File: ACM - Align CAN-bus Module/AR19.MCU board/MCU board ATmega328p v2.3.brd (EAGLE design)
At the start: 33.3 x 30.8 mm, 37 parts, among them IC1 ATMEGA328P-MMH, IC2 MIC5239-5.0YS_TR, IC3 MCP25625-E_ML, J1 AVR_SPI_PROG_3X2NS

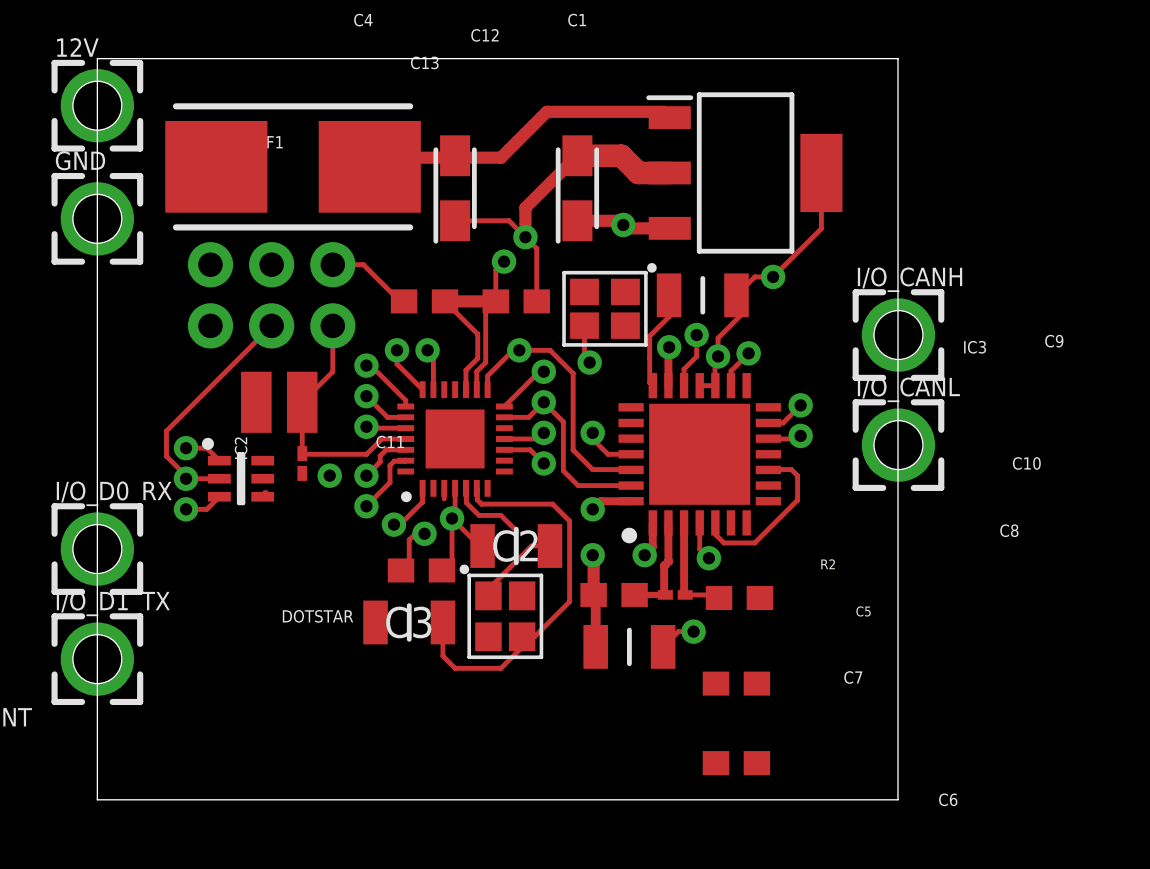
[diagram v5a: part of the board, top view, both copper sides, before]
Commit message: Removed: Extra GND connections
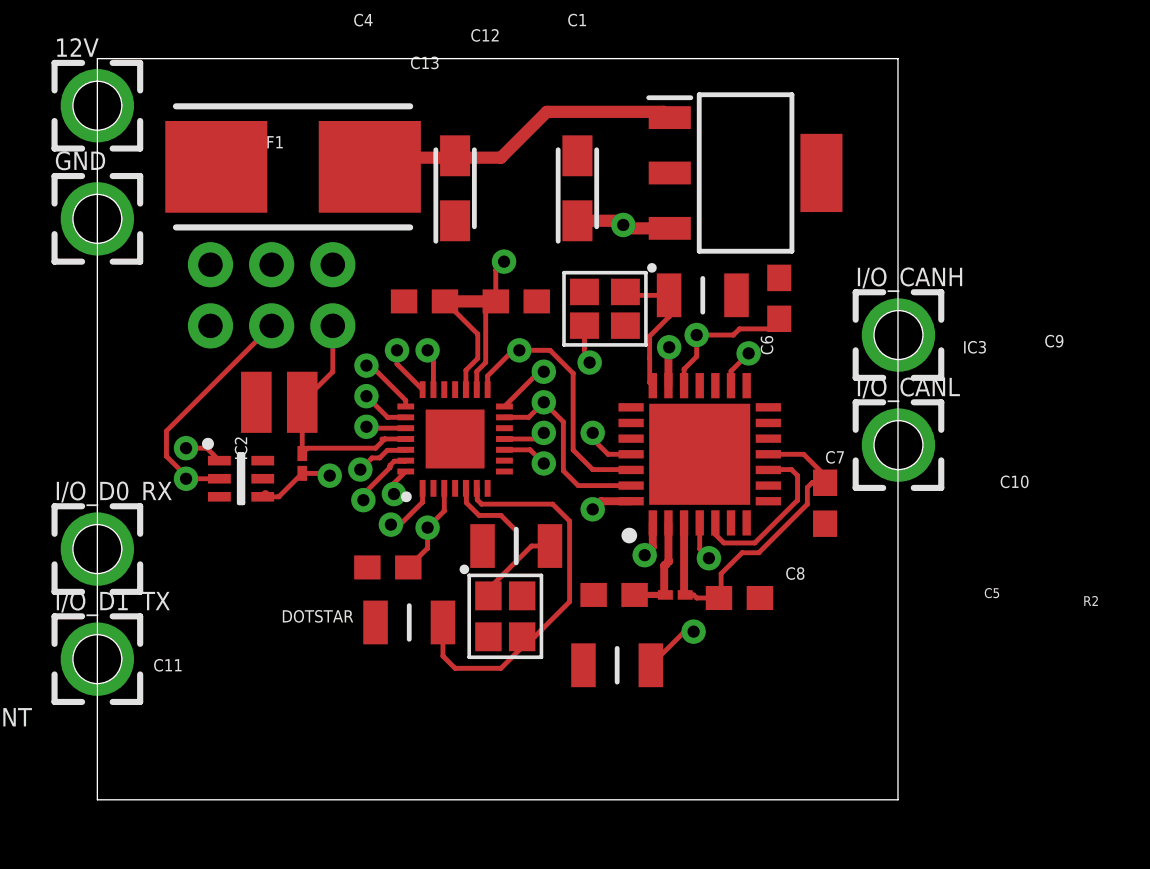
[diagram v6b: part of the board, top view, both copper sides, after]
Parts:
- moved C6 19.4 mm to (26.8, 20.8), turned to 90 degrees
- moved C7 8.35 mm to (28.7, 12.3), turned to 270 degrees
- moved C11 1.40 mm to (10.5, 9.65), turned to 180 degrees
- moved C10 0.92 mm to (20.1, 5.59)
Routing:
- net GND: track 40.9 -> 0.69 mm, vias 6 -> 0
- net 5V: track 50.3 -> 75.1 mm
- net CAN_INIT: track 2.11 -> 13.3 mm, vias 1 -> 2
- net CAN_OSC1: track 4.15 -> 6.02 mm
- net 12V_FUSED: track 11.8 -> 13.6 mm
- net CANH: track 1.64 -> 0.00 mm, vias 1 -> 0
- net CANL: track 1.40 -> 0.02 mm, vias 1 -> 0
- net RESET_MCU: track 9.15 -> 10.5 mm
- net CAN_OSC2: track 20.6 -> 21.4 mm

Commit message: Everything connected except GND and  5V Plane
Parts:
- moved I/O_AD1 91.7 mm to (32.5, 23.4)
- moved I/O_AD2 86.2 mm to (32.5, 19.6)
- moved I/O_AD3 79.8 mm to (32.5, 8.13)
- moved I/O_AD4_SDA 74.7 mm to (32.5, 4.32)
- moved I/O_AD5_SCL 40.0 mm to (-1.52, 19.6)
- moved GND 8.38 mm to (-1.52, 15.7)
- moved I/O_D2_INT 6.93 mm to (-1.52, 4.32)
- moved 12V 5.46 mm to (-1.52, 23.4), turned to 90 degrees
- moved C4 4.57 mm to (13.3, 20.8)
- moved C12 4.33 mm to (16.1, 16.4)
- moved C13 4.33 mm to (12.3, 16.4)
- moved DOTSTAR 4.33 mm to (4.70, 9.02)
- moved IC1 4.33 mm to (13.6, 10.7)
- moved IC2 4.33 mm to (25.7, 21.7)
- moved R1 4.33 mm to (7.24, 9.65)
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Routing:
- net I/O_AD4_SCL: track 2.00 -> 31.1 mm
- net I/O_AD3: track 2.49 -> 30.0 mm
- net I/O_AD2: track 2.07 -> 28.8 mm
- net I/O_AD1: track 1.73 -> 25.5 mm
- net I/O_AD5_SCL: track 1.66 -> 17.3 mm
- net I/O_D0_RX: track 10.2 -> 18.2 mm
- net I/O_D2_INT: track 8.79 -> 16.6 mm
- net CANH: track 0.00 -> 7.74 mm
- net CANL: track 0.02 -> 6.45 mm
- net 12V_UNFUSED: track 0.18 -> 5.16 mm
- net GND: track 0.69 -> 4.79 mm
- net I/O_D1_TX: track 15.1 -> 17.4 mm
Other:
- board size 33.3 x 30.8 mm -> 34.1 x 27.9 mm

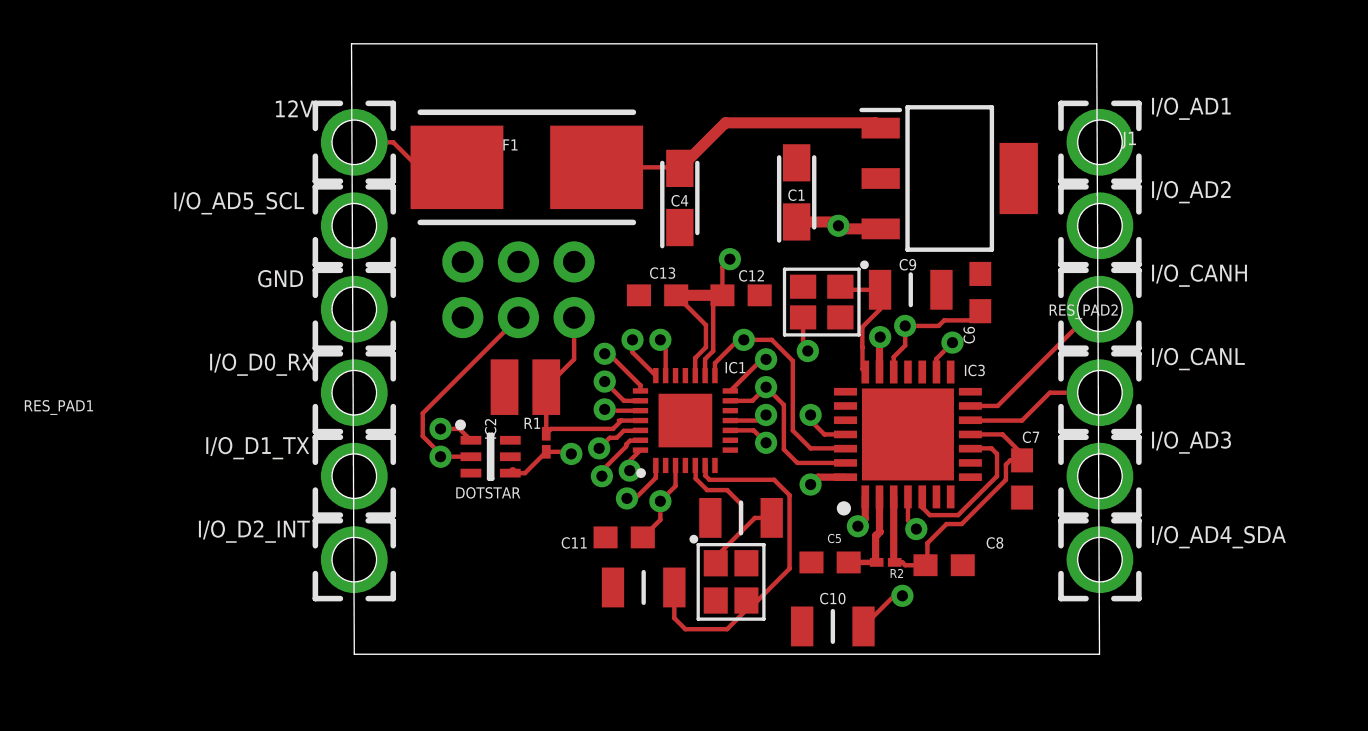
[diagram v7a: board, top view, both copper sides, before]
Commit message: Added: Ratsnest GND on Top and 4th Layer
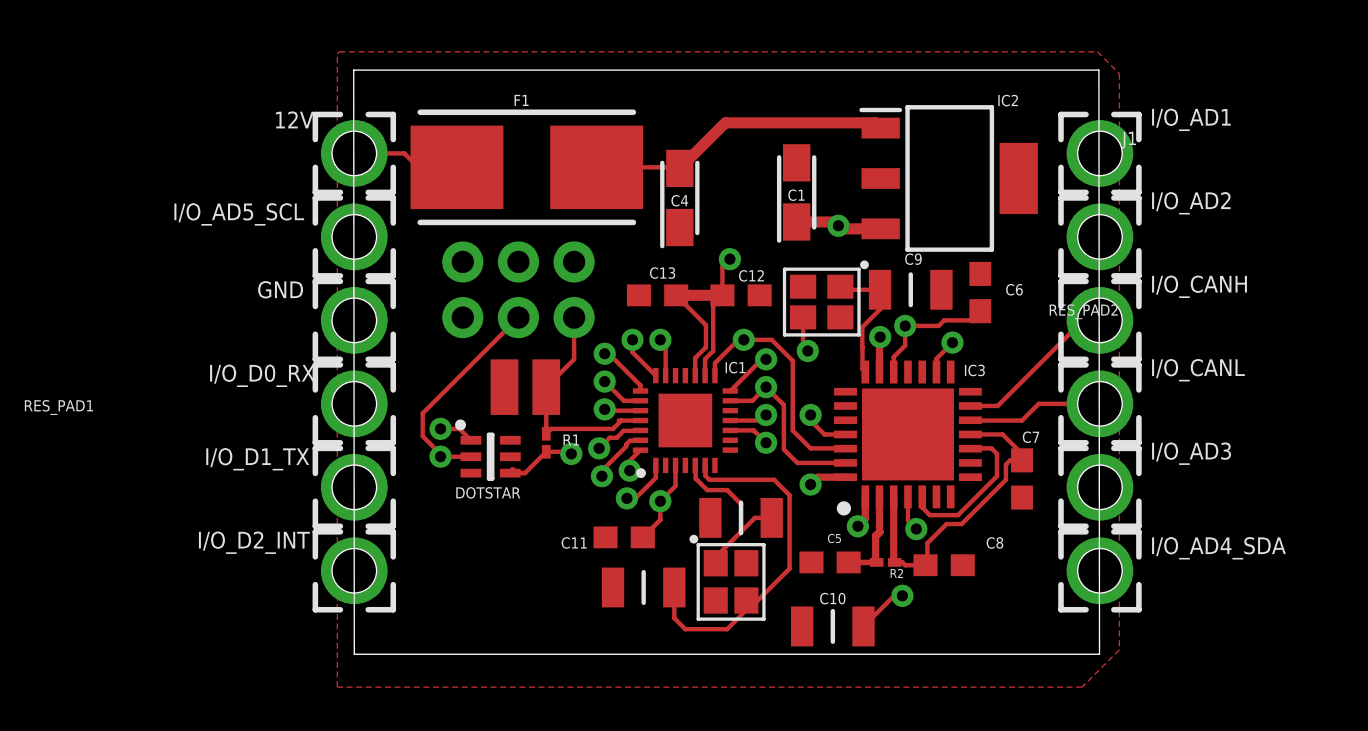
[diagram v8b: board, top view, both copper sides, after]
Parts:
- moved I/O_CANL 0.51 mm to (32.5, 11.4)
- moved I/O_D0_RX 0.51 mm to (-1.52, 11.4)
- moved I/O_AD3 0.51 mm to (32.5, 7.62)
- moved I/O_D1_TX 0.51 mm to (-1.52, 7.62)
- moved I/O_AD4_SDA 0.51 mm to (32.5, 3.81)
- moved I/O_D2_INT 0.51 mm to (-1.52, 3.81)
- moved 12V 0.51 mm to (-1.52, 22.9)
- moved GND 0.51 mm to (-1.52, 15.2)
- moved I/O_AD1 0.51 mm to (32.5, 22.9)
- moved I/O_AD2 0.51 mm to (32.5, 19.1)
- moved I/O_AD5_SCL 0.51 mm to (-1.52, 19.1)
- moved I/O_CANH 0.51 mm to (32.5, 15.2)
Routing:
- net I/O_D0_RX: track 18.2 -> 17.7 mm
- added copper zone on layer 1, net GND
- added copper zone on layer 4, net GND
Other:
- board size 34.1 x 27.9 mm -> 34 x 26.7 mm
